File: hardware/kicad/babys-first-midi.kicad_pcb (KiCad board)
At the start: 2 copper layers, 120 x 80 mm, 26 parts, among them J1 BFM:RJ45_Generic_THT, J2 Connector_Audio:TRS_3.5mm_Hor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, Q1 Package_TO_SOT_THT:TO-220-3_V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, Q2 Package_TO_SOT_THT:TO-220-3_V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, Q3 Package_TO_SOT_THT:TO-220-3_V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, Q4 Package_TO_SOT_THT:TO-220-3_V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, Q5 Package_TO_SOT_THT:TO-220-3_V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, U1 BFM:Pimoroni_Tiny2350_2x8_Hea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

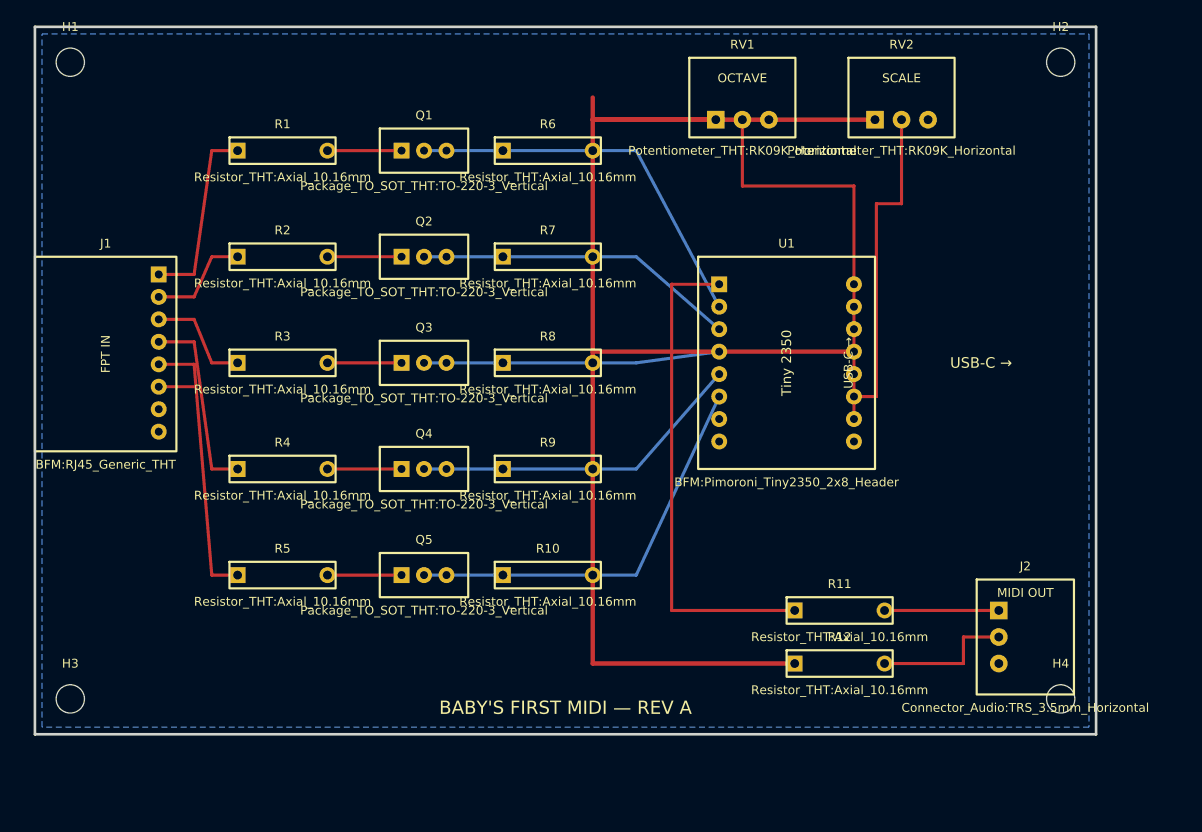
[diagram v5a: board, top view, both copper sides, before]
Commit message: Separate PCB routing into dedicated net corridors
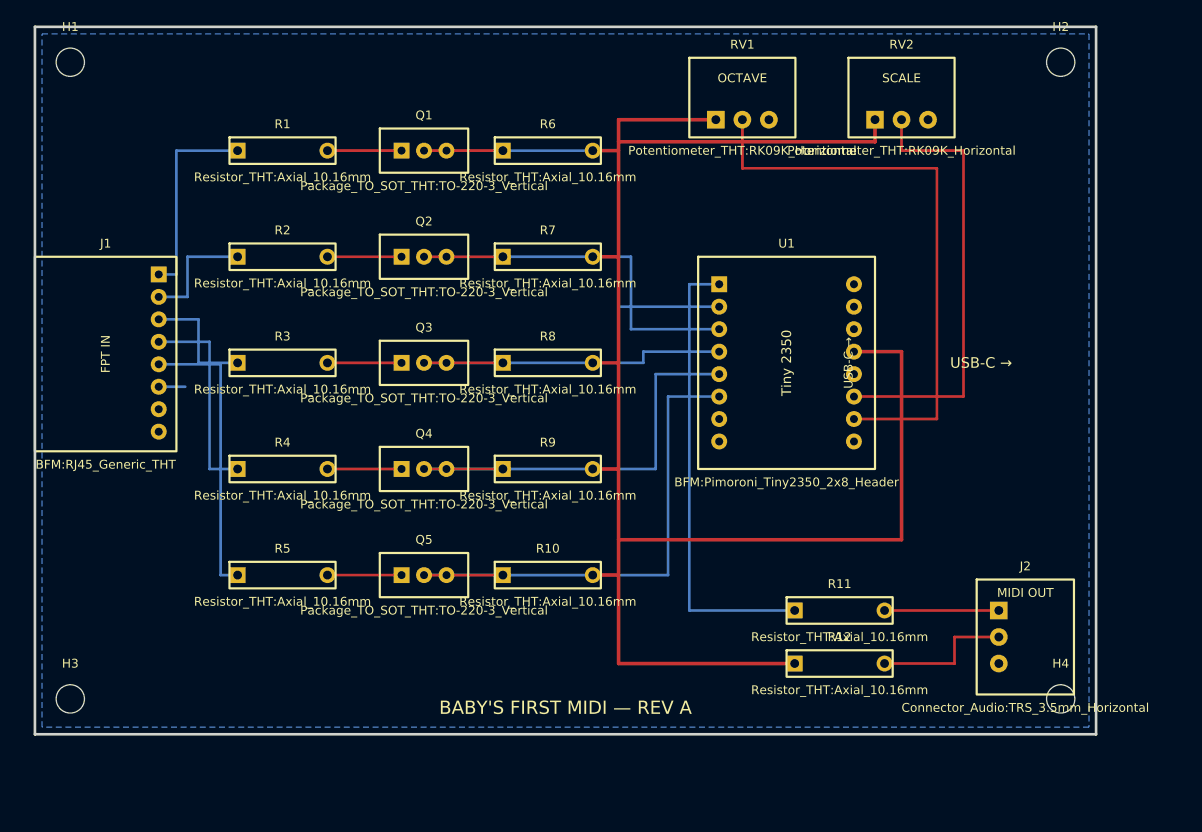
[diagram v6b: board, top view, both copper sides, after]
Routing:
- net 3V3: track 162.2 -> 197.2 mm
- net ADC_OCTAVE: track 46.5 -> 65.2 mm
- net KEY_G: track 46.3 -> 62.5 mm
- net KEY_C: track 44.0 -> 59.9 mm
- net KEY_F: track 38.3 -> 53.0 mm
- net KEY_D: track 36.5 -> 50.5 mm
- net ADC_SCALE: track 36.7 -> 50.7 mm
- net KEY_E: track 33.5 -> 43.6 mm
- net MIDI_TX: track 56.2 -> 52.2 mm
- net FPT_G: track 30.8 -> 32.8 mm
- net FPT_F: track 21.4 -> 23.3 mm
- net FPT_C: track 21.1 -> 22.9 mm
- net FPT_E: track 12.2 -> 13.8 mm
- net FPT_D: track 11.9 -> 13.5 mm
- net FPT_COMMON: track 4.00 -> 3.00 mm

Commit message: Rework PCB placement for clean routing
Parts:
- moved J1 114.2 mm to (135.5, 95.5)
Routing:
- net 3V3: track 197.2 -> 0.00 mm
- net ADC_OCTAVE: track 65.2 -> 0.00 mm
- net KEY_G: track 62.5 -> 0.00 mm
- net KEY_C: track 59.9 -> 0.00 mm
- net KEY_F: track 53.0 -> 0.00 mm
- net MIDI_TX: track 52.2 -> 0.00 mm
- net ADC_SCALE: track 50.7 -> 0.00 mm
- net KEY_D: track 50.5 -> 0.00 mm
- net KEY_E: track 43.6 -> 0.00 mm
- net FPT_G: track 32.8 -> 0.00 mm
- net FPT_F: track 23.3 -> 0.00 mm
- net FPT_C: track 22.9 -> 0.00 mm
- net MIDI_RING: track 15.9 -> 0.00 mm
- net FPT_E: track 13.8 -> 0.00 mm
- net FPT_D: track 13.5 -> 0.00 mm
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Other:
- board text added: "CONTROLS"
- board text added: "FPT INPUT"
- board text added: "INPUT BUFFERS"
- board text added: "MIDI OUT"
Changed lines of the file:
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@@
   (net 22 "MIDI_TIP")
   (net 23 "MIDI_RING")
-  (footprint "BFM:RJ45_Generic_THT" (layer "F.Cu") (at 28 57)
+  (footprint "BFM:RJ45_Generic_THT" (layer "F.Cu") (at 135.5 95.5 0)
     (property "Reference" "J1" (at 0 -12.5 0) (layer "F.SilkS") (effects (font (size 1 1) (thickness 0.15))))
     (property "Value" "BFM:RJ45_Generic_THT" (at 0 12.5 0) (layer "F.SilkS") (effects (font (size 1 1) (thickness 0.15))))
@@
   (gr_rect (start 20 20) (end 140 100) (stroke (width 0.3) (type default)) (fill none) (layer "Edge.Cuts"))
   (gr_text "BABY'S FIRST MIDI — REV A" (at 80 97) (layer "F.SilkS") (effects (font (size 1.5 1.5) (thickness 0.25))))
-  (gr_text "USB-C →" (at 127 58 0) (layer "F.SilkS") (effects (font (size 1.2 1.2) (thickness 0.2))))
-  (segment (start 34 48) (end 36 48) (width 0.3) (layer "B.Cu") (net 3))
-  (segment (start 36 48) (end 36 34) (width 0.3) (layer "B.Cu") (net 3))
-  (segment (start 36 34) (end 42.92 34) (width 0.3) (layer "B.Cu") (net 3))
-  (segment (start 53.08 34) (end 61.46 34) (width 0.3) (layer "F.Cu") (net 9))
-  (segment (start 64 34) (end 72.92 34) (width 0.3) (layer "F.Cu") (net 14))
-  (segment (start 34 50.54) (end 37.25 50.54) (width 0.3) (layer "B.Cu") (net 4))
-  (segment (start 37.25 50.54) (end 37.25 46) (width 0.3) (layer "B.Cu") (net 4))
-  (segment (start 37.25 46) (end 42.92 46) (width 0.3) (layer "B.Cu") (net 4))
-  (segment (start 53.08 46) (end 61.46 46) (width 0.3) (layer "F.Cu") (net 10))
-  (segment (start 64 46) (end 72.92 46) (width 0.3) (layer "F.Cu") (net 15))
-  (segment (start 34 53.08) (end 38.5 53.08) (width 0.3) (layer "B.Cu") (net 5))
-  (segment (start 38.5 53.08) (end 38.5 58) (width 0.3) (layer "B.Cu") (net 5))
-  (segment (start 38.5 58) (end 42.92 58) (width 0.3) (layer "B.Cu") (net 5))
-  (segment (start 53.08 58) (end 61.46 58) (width 0.3) (layer "F.Cu") (net 11))
-  (segment (start 64 58) (end 72.92 58) (width 0.3) (layer "F.Cu") (net 16))
-  (segment (start 34 55.62) (end 39.75 55.62) (width 0.3) (layer "B.Cu") (net 6))
-  (segment (start 39.75 55.62) (end 39.75 70) (width 0.3) (layer "B.Cu") (net 6))
-  (segment (start 39.75 70) (end 42.92 70) (width 0.3) (layer "B.Cu") (net 6))
-  (segment (start 53.08 70) (end 61.46 70) (width 0.3) (layer "F.Cu") (net 12))
-  (segment (start 64 70) (end 72.92 70) (width 0.3) (layer "F.Cu") (net 17))
-  (segment (start 34 58.16) (end 41 58.16) (width 0.3) (layer "B.Cu") (net 7))
-  (segment (start 41 58.16) (end 41 82) (width 0.3) (layer "B.Cu") (net 7))
-  (segment (start 41 82) (end 42.92 82) (width 0.3) (layer "B.Cu") (net 7))
-  (segment (start 53.08 82) (end 61.46 82) (width 0.3) (layer "F.Cu") (net 13))
-  (segment (start 64 82) (end 72.92 82) (width 0.3) (layer "F.Cu") (net 18))
-  (segment (start 64 34) (end 86 34) (width 0.3) (layer "B.Cu") (net 14))
-  (segment (start 86 34) (end 86 51.65) (width 0.3) (layer "B.Cu") (net 14))
-  (segment (start 86 51.65) (end 97.38 51.65) (width 0.3) (layer "B.Cu") (net 14))
-  (segment (start 64 46) (end 87.4 46) (width 0.3) (layer "B.Cu") (net 15))
-  (segment (start 87.4 46) (end 87.4 54.19) (width 0.3) (layer "B.Cu") (net 15))
-  (segment (start 87.4 54.19) (end 97.38 54.19) (width 0.3) (layer "B.Cu") (net 15))
-  (segment (start 64 58) (end 88.8 58) (width 0.3) (layer "B.Cu") (net 16))
-  (segment (start 88.8 58) (end 88.8 56.73) (width 0.3) (layer "B.Cu") (net 16))
-  (segment (start 88.8 56.73) (end 97.38 56.73) (width 0.3) (layer "B.Cu") (net 16))
-  (segment (start 64 70) (end 90.2 70) (width 0.3) (layer "B.Cu") (net 17))
-  (segment (start 90.2 70) (end 90.2 59.27) (width 0.3) (layer "B.Cu") (net 17))
-  (segment (start 90.2 59.27) (end 97.38 59.27) (width 0.3) (layer "B.Cu") (net 17))
-  (segment (start 64 82) (end 91.6 82) (width 0.3) (layer "B.Cu") (net 18))
-  (segment (start 91.6 82) (end 91.6 61.81) (width 0.3) (layer "B.Cu") (net 18))
-  (segment (start 91.6 61.81) (end 97.38 61.81) (width 0.3) (layer "B.Cu") (net 18))
-  (segment (start 83.08 34) (end 86 34) (width 0.4) (layer "F.Cu") (net 2))
-  (segment (start 83.08 46) (end 86 46) (width 0.4) (layer "F.Cu") (net 2))
-  (segment (start 83.08 58) (end 86 58) (width 0.4) (layer "F.Cu") (net 2))
-  (segment (start 83.08 70) (end 86 70) (width 0.4) (layer "F.Cu") (net 2))
-  (segment (start 83.08 82) (end 86 82) (width 0.4) (layer "F.Cu") (net 2))
-  (segment (start 86 30.5) (end 86 92) (width 0.4) (layer "F.Cu") (net 2))
-  (segment (start 97 30.5) (end 86 30.5) (width 0.4) (layer "F.Cu") (net 2))
-  (segment (start 115 30.5) (end 115 33) (width 0.4) (layer "F.Cu") (net 2))
-  (segment (start 115 33) (end 86 33) (width 0.4) (layer "F.Cu") (net 2))
-  (segment (start 112.62 56.73) (end 118 56.73) (width 0.4) (layer "F.Cu") (net 2))
-  (segment (start 118 56.73) (end 118 78) (width 0.4) (layer "F.Cu") (net 2))
-  (segment (start 118 78) (end 86 78) (width 0.4) (layer "F.Cu") (net 2))
-  (segment (start 105.92 92) (end 86 92) (width 0.4) (layer "F.Cu") (net 2))
-  (segment (start 112.62 64.35) (end 122 64.35) (width 0.3) (layer "F.Cu") (net 20))
-  (segment (start 122 64.35) (end 122 36) (width 0.3) (layer "F.Cu") (net 20))
-  (segment (start 122 36) (end 100 36) (width 0.3) (layer "F.Cu") (net 20))
-  (segment (start 100 36) (end 100 30.5) (width 0.3) (layer "F.Cu") (net 20))
-  (segment (start 112.62 61.81) (end 125 61.81) (width 0.3) (layer "F.Cu") (net 21))
-  (segment (start 125 61.81) (end 125 34) (width 0.3) (layer "F.Cu") (net 21))
-  (segment (start 125 34) (end 118 34) (width 0.3) (layer "F.Cu") (net 21))
-  (segment (start 118 34) (end 118 30.5) (width 0.3) (layer "F.Cu") (net 21))
-  (segment (start 97.38 49.11) (end 94 49.11) (width 0.3) (layer "B.Cu") (net 19))
-  (segment (start 94 49.11) (end 94 86) (width 0.3) (layer "B.Cu") (net 19))
-  (segment (start 94 86) (end 105.92 86) (width 0.3) (layer "B.Cu") (net 19))
-  (segment (start 116.08 86) (end 129 86) (width 0.3) (layer "F.Cu") (net 22))
-  (segment (start 116.08 92) (end 124 92) (width 0.3) (layer "F.Cu") (net 23))
-  (segment (start 124 92) (end 124 89) (width 0.3) (layer "F.Cu") (net 23))
-  (segment (start 124 89) (end 129 89) (width 0.3) (layer "F.Cu") (net 23))
-  (segment (start 34 60.7) (end 37 60.7) (width 0.3) (layer "B.Cu") (net 8))
+  (gr_text "USB-C →" (at 128 56 0) (layer "F.SilkS") (effects (font (size 1.2 1.2) (thickness 0.2))))
+  (gr_text "FPT INPUT" (at 29 42 90) (layer "F.SilkS") (effects (font (size 1.1 1.1) (thickness 0.2))))
+  (gr_text "INPUT BUFFERS" (at 62 25) (layer "F.SilkS") (effects (font (size 1.1 1.1) (thickness 0.2))))
+  (gr_text "CONTROLS" (at 105 21.5) (layer "F.SilkS") (effects (font (size 1.0 1.0) (thickness 0.18))))
+  (gr_text "MIDI OUT" (at 124 78) (layer "F.SilkS") (effects (font (size 1.0 1.0) (thickness 0.18))))
   (zone (net 1) (net_name "GND") (layer "B.Cu") (hatch edge 0.5)
     (connect_pads (clearance 0.5))
